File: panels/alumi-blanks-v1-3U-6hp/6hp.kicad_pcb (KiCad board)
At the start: 2 copper layers, 30 x 128.5 mm, 2 parts

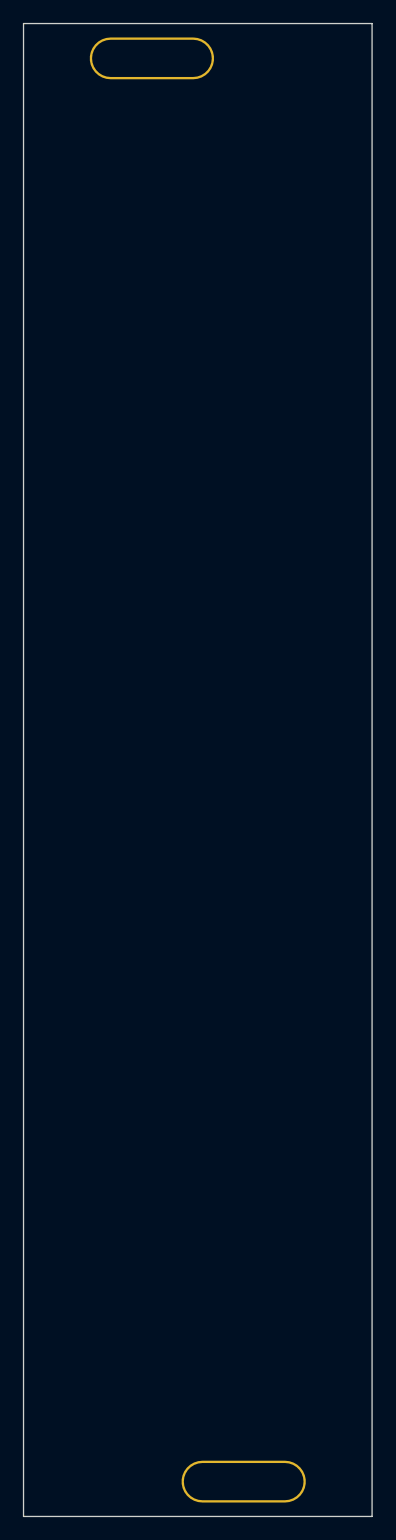
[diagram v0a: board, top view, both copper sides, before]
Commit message: feat: add new screw hole footprints and update panel KiCad files for new JLCPCB order
- Added modular-3M-screw-hole-size1-alumi-0604, modular-3M-screw-hole-size1-fit-alumi-0604, modular-3M-screw-hole-size2-alumi-0604
- Updated all panel .kicad_pcb and .kicad_pro files for 3U panels (1hp-16hp)
- Added new JLCPCB order snapshot and Gerber outputs

Co-authored-by: Copilot <223556219+Copilot@users.noreply.github.com>
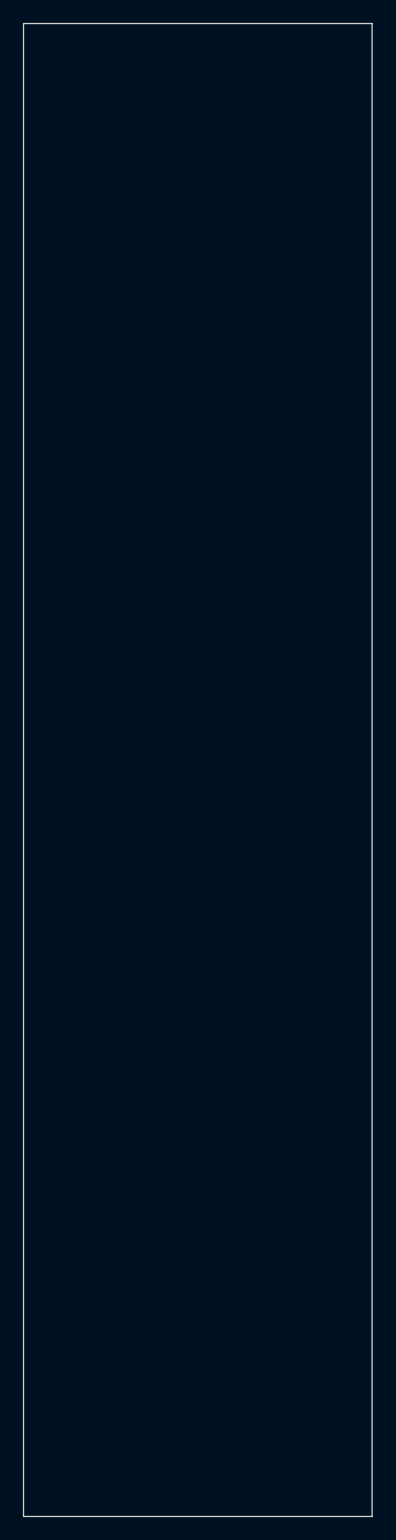
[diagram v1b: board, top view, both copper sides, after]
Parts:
- removed the REF** at (11.1, 3.00)
- removed the REF** at (18.9, 125.5)
- added REF**: modular-3M-screw-hole-size2-alumi-0604, zudo-blanks:modular-3M-screw-hole-size2-alumi-0604, F.Cu at (19.8, 125.5)
- added REF**: modular-3M-screw-hole-size2-alumi-0604, zudo-blanks:modular-3M-screw-hole-size2-alumi-0604, F.Cu at (10.2, 3.00)
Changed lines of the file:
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@@
 (kicad_pcb
-	(version 20240108)
+	(version 20260206)
 	(generator "pcbnew")
-	(generator_version "8.0")
+	(generator_version "10.0")
 	(general
 		(thickness 1.6)
@@
 	(layers
 		(0 "F.Cu" signal)
-		(31 "B.Cu" signal)
-		(32 "B.Adhes" user "B.Adhesive")
-		(33 "F.Adhes" user "F.Adhesive")
-		(34 "B.Paste" user)
-		(35 "F.Paste" user)
-		(36 "B.SilkS" user "B.Silkscreen")
-		(37 "F.SilkS" user "F.Silkscreen")
-		(38 "B.Mask" user)
-		(39 "F.Mask" user)
-		(40 "Dwgs.User" user "User.Drawings")
-		(41 "Cmts.User" user "User.Comments")
-		(42 "Eco1.User" user "User.Eco1")
-		(43 "Eco2.User" user "User.Eco2")
-		(44 "Edge.Cuts" user)
-		(45 "Margin" user)
-		(46 "B.CrtYd" user "B.Courtyard")
-		(47 "F.CrtYd" user "F.Courtyard")
-		(48 "B.Fab" user)
-		(49 "F.Fab" user)
-		(50 "User.1" user)
-		(51 "User.2" user)
-		(52 "User.3" user)
-		(53 "User.4" user)
-		(54 "User.5" user)
-		(55 "User.6" user)
-		(56 "User.7" user)
-		(57 "User.8" user)
-		(58 "User.9" user)
+		(2 "B.Cu" signal)
+		(9 "F.Adhes" user "F.Adhesive")
+		(11 "B.Adhes" user "B.Adhesive")
+		(13 "F.Paste" user)
+		(15 "B.Paste" user)
+		(5 "F.SilkS" user "F.Silkscreen")
+		(7 "B.SilkS" user "B.Silkscreen")
+		(1 "F.Mask" user)
+		(3 "B.Mask" user)
+		(17 "Dwgs.User" user "User.Drawings")
+		(19 "Cmts.User" user "User.Comments")
+		(21 "Eco1.User" user "User.Eco1")
+		(23 "Eco2.User" user "User.Eco2")
+		(25 "Edge.Cuts" user)
+		(27 "Margin" user)
+		(31 "F.CrtYd" user "F.Courtyard")
+		(29 "B.CrtYd" user "B.Courtyard")
+		(35 "F.Fab" user)
+		(33 "B.Fab" user)
+		(39 "User.1" user)
+		(41 "User.2" user)
+		(43 "User.3" user)
+		(45 "User.4" user)
+		(47 "User.5" user)
+		(49 "User.6" user)
+		(51 "User.7" user)
+		(53 "User.8" user)
+		(55 "User.9" user)
 	)
 	(setup
 		(pad_to_mask_clearance 0)
 		(allow_soldermask_bridges_in_footprints no)
+		(tenting
+			(front yes)
+			(back yes)
+		)
+		(covering
+			(front no)
+			(back no)
+		)
+		(plugging
+			(front no)
+			(back no)
+		)
+		(capping no)
+		(filling no)
 		(pcbplotparams
-			(layerselection 0x00010fc_ffffffff)
-			(plot_on_all_layers_selection 0x0000000_00000000)
+			(layerselection 0x00000000_00000000_55555555_5755555a)
+			(plot_on_all_layers_selection 0x00000000_00000000_00000000_00000000)
 			(disableapertmacros no)
 			(usegerberextensions no)
@@
 			(usegerberadvancedattributes yes)
 			(creategerberjobfile yes)
-			(dashed_line_dash_ratio 12.000000)
-			(dashed_line_gap_ratio 3.000000)
+			(dashed_line_dash_ratio 12)
+			(dashed_line_gap_ratio 3)
 			(svgprecision 4)
 			(plotframeref no)
-			(viasonmask no)
 			(mode 1)
 			(useauxorigin no)
-			(hpglpennumber 1)
-			(hpglpenspeed 20)
-			(hpglpendiameter 15.000000)
 			(pdf_front_fp_property_popups yes)
 			(pdf_back_fp_property_popups yes)
+			(pdf_metadata yes)
+			(pdf_single_document no)
 			(dxfpolygonmode yes)
 			(dxfimperialunits yes)
@@
 			(psnegative no)
 			(psa4output no)
-			(plotreference yes)
-			(plotvalue yes)
-			(plotfptext yes)
-			(plotinvisibletext no)
+			(plot_black_and_white yes)
 			(sketchpadsonfab no)
+			(plotpadnumbers no)
+			(hidednponfab no)
+			(sketchdnponfab yes)
+			(crossoutdnponfab yes)
 			(subtractmaskfromsilk no)
 			(outputformat 1)
@@
 		)
 	)
-	(net 0 "")
-	(footprint "Library:blankPanelHole"
+	(footprint "zudo-blanks:modular-3M-screw-hole-size2-alumi-0604"
 		(layer "F.Cu")
-		(at 11.05 3)
+		(at 19.84 125.5)
 		(property "Reference" "REF**"
 			(at 0 -0.5 0)
@@
 			)
 		)
-		(property "Value" "blankPanelHole"
+		(property "Value" "modular-3M-screw-hole-size2-alumi-0604"
 			(at 0 1 0)
 			(unlocked yes)
@@
 			)
 		)
-		(property "Footprint" "Library:blankPanelHole"
-			(at 0 0 0)
-			(unlocked yes)
-			(layer "F.Fab")
-			(hide yes)
-			(effects
-				(font
-					(size 1 1)
-					(thickness 0.15)
-				)
-			)
-		)
 		(property "Datasheet" ""
 			(at 0 0 0)
@@
 			)
 		)
-		(attr through_hole)
-		(pad "1" thru_hole roundrect
+		(attr smd)
+		(duplicate_pad_numbers_are_jumpers no)
+		(pad "" np_thru_hole roundrect
 			(at 0 0 90)
-			(size 3.6 10.7)
-			(drill oval 3.2 10.3)
-			(layers "*.Cu" "*.Mask")
-			(remove_unused_layers no)
-			(roundrect_rratio 0.5)
-		)
-	)
-	(footprint "Library:blankPanelHole"
+			(size 4 11.08)
+			(drill oval 3.2 10.28)
+			(layers "*.Mask")
+			(roundrect_rratio 0.4998750312)
+		)
+		(embedded_fonts no)
+	)
+	(footprint "zudo-blanks:modular-3M-screw-hole-size2-alumi-0604"
 		(layer "F.Cu")
-		(at 18.95 125.5)
+		(at 10.16 3)
 		(property "Reference" "REF**"
 			(at 0 -0.5 0)
@@
 			)
 		)
-		(property "Value" "blankPanelHole"
+		(property "Value" "modular-3M-screw-hole-size2-alumi-0604"
 			(at 0 1 0)
 			(unlocked yes)
@@
 			)
 		)
-		(property "Footprint" "Library:blankPanelHole"
-			(at 0 0 0)
-			(unlocked yes)
-			(layer "F.Fab")
-			(hide yes)
-			(effects
-				(font
-					(size 1 1)
-					(thickness 0.15)
-				)
-			)
-		)
 		(property "Datasheet" ""
 			(at 0 0 0)
@@
 			)
 		)
-		(attr through_hole)
-		(pad "1" thru_hole roundrect
+		(attr smd)
+		(duplicate_pad_numbers_are_jumpers no)
+		(pad "" np_thru_hole roundrect
 			(at 0 0 90)
-			(size 3.6 10.7)
-			(drill oval 3.2 10.3)
-			(layers "*.Cu" "*.Mask")
-			(remove_unused_layers no)
-			(roundrect_rratio 0.5)
-		)
-	)
-	(gr_poly
-		(pts
-			(xy 29.999807 128.498764) (xy 0 128.498764) (xy 0 0.001239) (xy 29.999807 0.001239)
-		)
-		(stroke
-			(width -0.000001)
-			(type solid)
-		)
-		(fill solid)
+			(size 4 11.08)
+			(drill oval 3.2 10.28)
+			(layers "*.Mask")
+			(roundrect_rratio 0.4998750312)
+		)
+		(embedded_fonts no)
+	)
+	(gr_rect
+		(start 0 0)
+		(end 30 128.5)
+		(stroke
+			(width 0.05)
+			(type solid)
+		)
+		(fill no)
 		(layer "Edge.Cuts")
 	)
 	(gr_poly
 		(pts
+			(xy 5.70081 30.001047) (xy 0 30.001047) (xy 0 0.001239) (xy 5.70081 0.001239)
+		)
+		(stroke
+			(width -0.000001)
+			(type solid)
+		)
+		(fill yes)
+		(layer "User.1")
+	)
+	(gr_poly
+		(pts
+			(xy 29.999804 128.498764) (xy 24.298996 128.498764) (xy 24.298996 98.498955) (xy 29.999804 98.498955)
+		)
+		(stroke
+			(width -0.000001)
+			(type solid)
+		)
+		(fill yes)
+		(layer "User.1")
+	)
+	(gr_poly
+		(pts
+			(xy 29.999807 1.200667) (xy 0 1.200667) (xy 0 0.001239) (xy 29.999807 0.001239)
+		)
+		(stroke
+			(width -0.000001)
+			(type solid)
+		)
+		(fill yes)
+		(layer "User.1")
+	)
+	(gr_poly
+		(pts
 			(xy 29.999807 128.498764) (xy 0 128.498764) (xy 0 127.299339) (xy 29.999807 127.299339)
 		)
@@
 			(type solid)
 		)
-		(fill solid)
-		(layer "User.1")
-	)
-	(gr_poly
-		(pts
-			(xy 5.70081 30.001047) (xy 0 30.001047) (xy 0 0.001239) (xy 5.70081 0.001239)
-		)
-		(stroke
-			(width -0.000001)
-			(type solid)
-		)
-		(fill solid)
-		(layer "User.1")
-	)
-	(gr_poly
-		(pts
-			(xy 29.999807 1.200667) (xy 0 1.200667) (xy 0 0.001239) (xy 29.999807 0.001239)
-		)
-		(stroke
-			(width -0.000001)
-			(type solid)
-		)
-		(fill solid)
-		(layer "User.1")
-	)
-	(gr_poly
-		(pts
-			(xy 29.999804 128.498764) (xy 24.298996 128.498764) (xy 24.298996 98.498955) (xy 29.999804 98.498955)
-		)
-		(stroke
-			(width -0.000001)
-			(type solid)
-		)
-		(fill solid)
-		(layer "User.1")
-	)
+		(fill yes)
+		(layer "User.1")
+	)
+	(embedded_fonts no)
 )
